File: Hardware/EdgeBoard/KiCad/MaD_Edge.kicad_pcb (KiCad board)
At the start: 4 copper layers, 144.1 x 93.3 mm, 281 parts, among them IC1 ISO6742DWR, IC10 NSI50010YT1G, IC11 NSI50010YT1G, IC12 NSI50010YT1G, IC13 NSI50010YT1G, IC14 ISO7741FDWR, IC15 ISO6721BDR, IC16 ISO6740FDWR, IC2 ISO6742DWR, IC3 UCC12040DVER, IC4 UCC12040DVER, IC5 ISO6731DWR, IC6 NSI50010YT1G, IC7 NSI50010YT1G, IC8 NSI50010YT1G, IC9 NSI50010YT1G, J1 Debug, J10 ChargePump, J11 ESDUpper, J12 ESDLower, J13 ESDActive, J14 ENDUpper, J15 ENDLower, J16 Door, J17 GPI_3, J18 GPI_4, J19 NavKey, J2 Main_Power, J20 Encoder, J21 ServoCtrl, J22 GPIO_EXT_1, J23 ServoSerial, J24 GPIO_EXT_2, J3 P2_EDGE_MODULE_SOCKET, J4 436500321, J5 GPO_2, J6 GPO_1, J7 GPI_2, J8 GPI_1, J9 Force, Q1 MMBT3904, SW1 RESET, U1 XL1509-5V, U10 SN74LVC1G14DBV, U11 SN74LVC1G14DBV, U12 SN74LVC1G14DBV, U13 SN74LVC1G14DBV, U14 SN74LVC1G14DBV, U15 SN74LVC1G14DBV, U16 SN74LVC1G14DBV, U17 SN74LVC1G14DBV, U18 SN74LVC1G14DBV, U19 SN74LVC1G14DBV, U2 XL1509-3.3V, U21 SN74LVC1G14DBV, U22 SN74LVC1G14DBV, U24 AM26LS31CD, U25 AM26C32IDR, U27 SN74LVC1G14DBV, U28 SN74LVC1G14DBV, U29 SN74LVC1G14DBV, U3 APM4953, U30 SN74LVC1G14DBV, U31 SN74LVC1G14DBV, U32 SN74LVC1G14DBV, U33 SN74LVC1G14DBV, U34 SN74LVC1G14DBV, U4 6N137, U5 VO2631, U6 VO2631, U7 VO2631, U8 VO2631, U9 SN74LVC1G14DBV

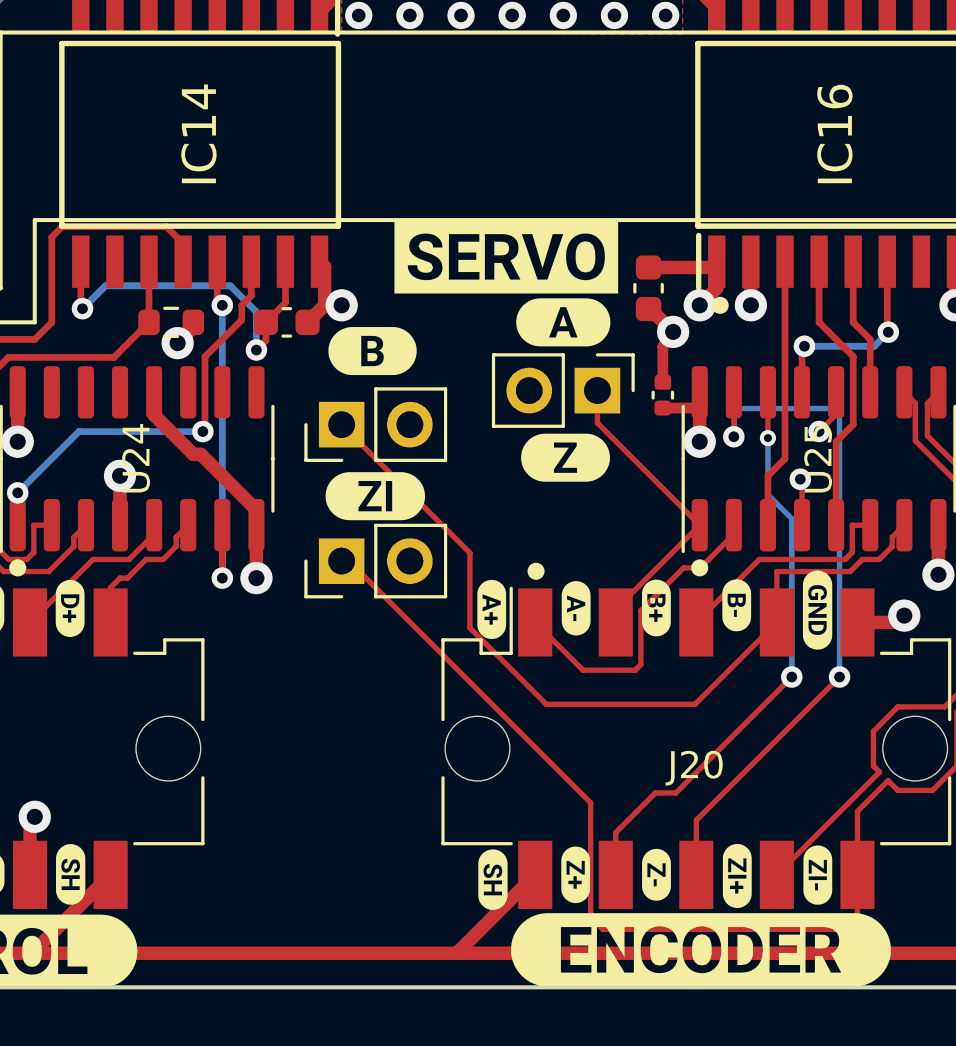
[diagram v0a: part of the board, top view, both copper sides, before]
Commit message: feat(hardware): encoder front end for single-ended and open-collector encoders
Findings ENC-F4a and ENC-F4b. Grounding a minus input can never give the
-0.2 V differential low (SLLS104M 5.6 p.5), and the Taiss NPN
open-collector encoder had no pull-up and no supply.

- JP2/JP3/JP5 now tie A-/B-/ZI- to ENC_REF instead of EN_GND (values
  A_REF/B_REF/ZI_REF); JP6 (Z_REF) is the Z- jumper where JP4 was.
- ENC_REF = SC_5V/2: R43/R44 2.2 k, C31 0.1 uF, placed between IC14 and
  IC16; B.Cu to the four jumpers.
- R40/R41/R42 2.2 k pull-ups on A+/B+/Z+ (an A/B/Z encoder). Placed
  between J21 and J20, tapped onto the + nets with vias and B.Cu.
- J25 (1x3 header: VIN, fused +V, 0V) with F1, Littelfuse 1206L020/30NR
  (C7542932; 0.20 A hold, 30 V, 1206L datasheet p.1), as an external
  supply pass-through: J20 has no free pin and the encoder side only has
  SC_5V from the drive.
- BOM: SH1-SH4, 2.54 mm shunts (HC-JP254-1-65-CL-B-G0, C5380290) for
  JP1 (always) and JP2/JP3/JP6 (open-collector encoder only), as
  BOM-only symbols.
- Silkscreen: SERVO label moved up 2.2 mm; VIN/+V/0V at J25; SHUNT=OC
  between the jumpers.

Co-Authored-By: Claude Opus 5.5 <noreply@anthropic.com>
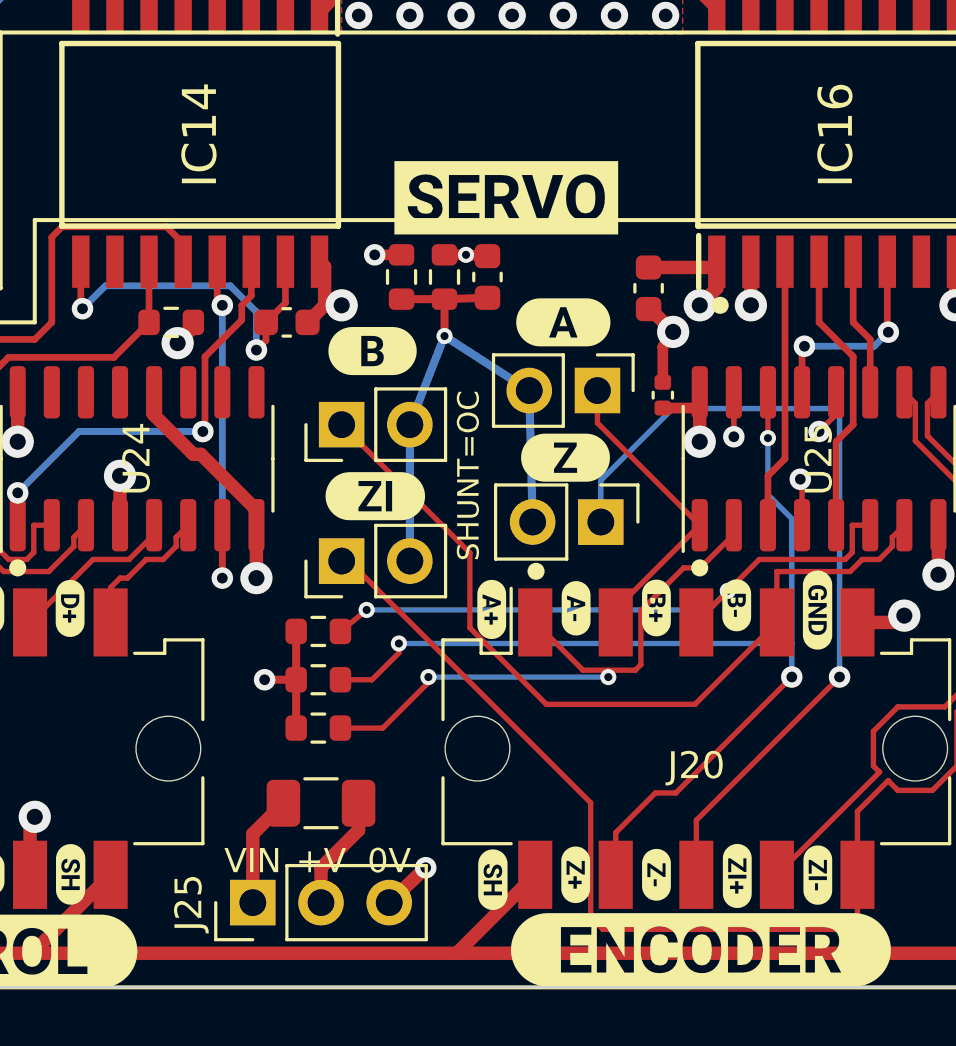
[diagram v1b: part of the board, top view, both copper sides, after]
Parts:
- added C31: 0.1uF, Capacitor_SMD:C_0603_1608Metric, F.Cu at (44.8, 185.0)
- added F1: 0.2A/30V, Fuse:Fuse_1206_3216Metric, F.Cu at (38.6, 204.6)
- added J25: ENC_PWR, Connector_PinHeader_2.54mm:PinHeader_1x03_P2.54mm_Vertical, F.Cu at (36.1, 208.3)
- added JP6: Z_REF, Connector_PinHeader_2.54mm:PinHeader_1x02_P2.54mm_Vertical, F.Cu at (49.0, 194.1)
- added R40: 2.2K, Resistor_SMD:R_0603_1608Metric, F.Cu at (38.5, 201.8)
- added R41: 2.2K, Resistor_SMD:R_0603_1608Metric, F.Cu at (38.5, 198.2)
- added R42: 2.2K, Resistor_SMD:R_0603_1608Metric, F.Cu at (38.5, 200.0)
- added R43: 2.2K, Resistor_SMD:R_0603_1608Metric, F.Cu at (41.6, 185.0)
- added R44: 2.2K, Resistor_SMD:R_0603_1608Metric, F.Cu at (43.2, 185.0)
- JP2: value A_GND -> A_REF
- JP3: value B_GND -> B_REF
- JP5: value ZI_GND -> ZI_REF
- moved kibuzzard-6474D3A4 2.20 mm to (45.5, 182.1)
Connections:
- JP2 pad 2: /MaD_Edge_Sheet3/EN_GND -> /MaD_Edge_Sheet3/ENC_REF
- JP3 pad 2: /MaD_Edge_Sheet3/EN_GND -> /MaD_Edge_Sheet3/ENC_REF
- JP5 pad 2: /MaD_Edge_Sheet3/EN_GND -> /MaD_Edge_Sheet3/ENC_REF
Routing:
- net /MaD_Edge_Sheet3/ENC_REF: track 0.00 -> 21.8 mm, vias 0 -> 1
- net /MaD_Edge_Sheet3/Z+: track 21.5 -> 39.1 mm, vias 2 -> 3
- net /MaD_Edge_Sheet3/B+: track 8.57 -> 23.6 mm, vias 0 -> 2
- net /MaD_Edge_Sheet3/A+: track 11.7 -> 22.9 mm, vias 0 -> 2
- net /MaD_Edge_Sheet3/Z-: track 26.2 -> 33.8 mm
- net /MaD_Edge_Sheet3/SC_5V: track 19.7 -> 25.5 mm, vias 8 -> 10
- net /MaD_Edge_Sheet3/ENC_V+: track 0.00 -> 4.28 mm
- net /MaD_Edge_Sheet3/ENC_VIN: track 0.00 -> 4.17 mm
- net /MaD_Edge_Sheet3/EN_GND: track 40.4 -> 43.8 mm, vias 12 -> 14
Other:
- board text added: "+V"
- board text added: "0V"
- board text added: "SHUNT=OC"
- board text added: "VIN"

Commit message: fix(hardware): Pi link on P29-P32 and a 3.3 V Pi side
Findings HOST-F2 and HOST-F5. The P2-EC32MB does not bring out P40-P57
(fingers 59-62 are no-connects), so IC2 on P52-P55 was dead, and the Pi
side ran from 5 V, putting about 5 V on Pi GPIO.

- IC2 INA/INB/OUTC/OUTD move to P32/P31/P30/P29. P29-P31 are the only
  EC32MB pins the carrier leaves unused; the fourth (an isolator input,
  10 uA max, SLLSFJ6G p.12) shares P32 with J22.3.
- Routes: the old P52-P55 copper is removed; IC2 to four vias, B.Cu down
  to J22.3 (P32) and to vias in J3 fingers 9-11 (the only access).
- RPI_5V renamed RPI_3V3 (pads, tracks, In2 plane); J4.1 silkscreen
  reads 3V3. ISO674x runs at 2.25-5.5 V with VIT+ = 0.7 VCCI (SLLSFJ6G
  p.8, p.12).
- IC2 alternate ISO7742FDWR dropped: a default-low output would hold the
  UART low (SLLSFJ6G p.31).

Firmware follow-up: HW_PIN_RPI_TX 55 -> 32, HW_PIN_RPI_RX 53 -> 30.

Co-Authored-By: Claude Opus 5.5 <noreply@anthropic.com>
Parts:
- removed kibuzzard-6477790B: G***, kibuzzard-6477790B
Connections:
- net /MaD_Edge_Sheet2/RPI_5V renamed /MaD_Edge_Sheet2/RPI_3V3
- IC2 pad 3: P55 -> P32
- IC2 pad 4: P54 -> P31
- IC2 pad 5: P53 -> P30
- IC2 pad 6: P52 -> P29
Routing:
- net P32: track 3.09 -> 56.9 mm, vias 0 -> 1
- net P29: track 0.00 -> 53.8 mm, vias 0 -> 2
- net P30: track 0.00 -> 53.2 mm, vias 0 -> 2
- net P31: track 0.00 -> 52.6 mm, vias 0 -> 2
- net P55: track 49.3 -> 0.00 mm
- net P54: track 47.5 -> 0.00 mm
- net P52: track 46.9 -> 0.00 mm
- net P53: track 45.9 -> 0.00 mm

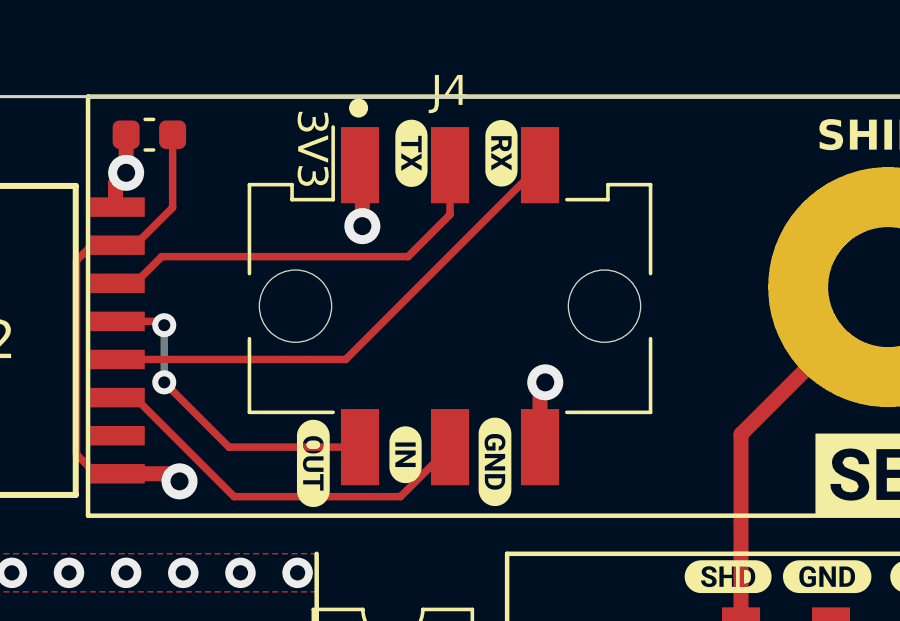
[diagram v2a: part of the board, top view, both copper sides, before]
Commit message: fix(hardware): J4 back on the 43045-0618 footprint
Finding HOST-J4. J4's BOM part is 0430450618 (with solder tabs) and the
2023 board used the 43045-0618 footprint; the current files had 0615
(no tabs). The library footprint drops in at the same place: its two
mounting pads clear all copper (checked against every F.Cu item with
0.2 mm clearance). The tabs stay unnumbered as in 2023, so the DRC
parity note about J4 pin 7 (SHIELD) is unchanged.

Co-Authored-By: Claude Opus 5.5 <noreply@anthropic.com>
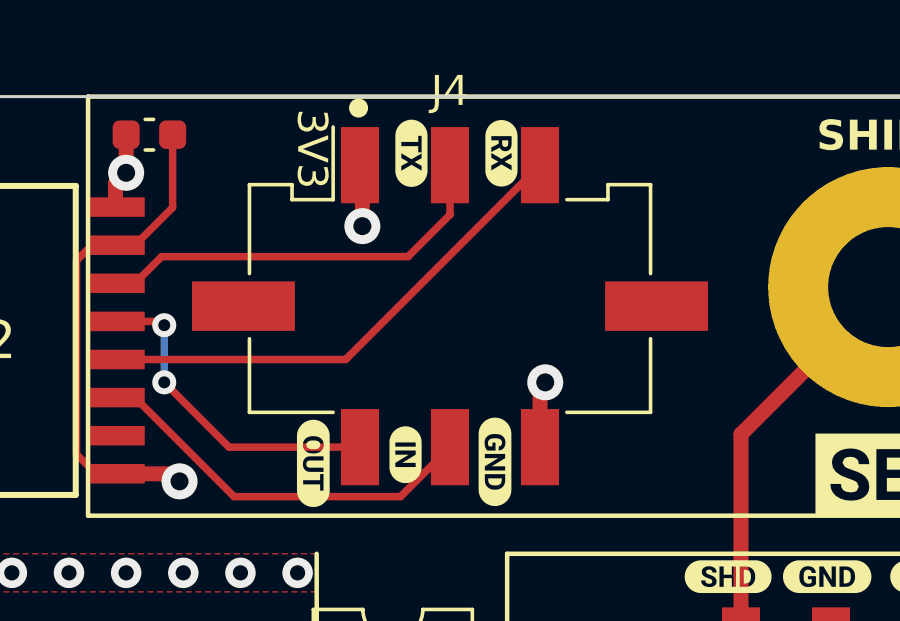
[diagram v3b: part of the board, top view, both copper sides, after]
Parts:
- J4: footprint Connector_Molex:Molex_Micro-Fit_3.0_43045-0615_2x03_P3.00mm_Vertical -> Connector_Molex:Molex_Micro-Fit_3.0_43045-0618_2x03-1MP_P3.00mm_Vertical

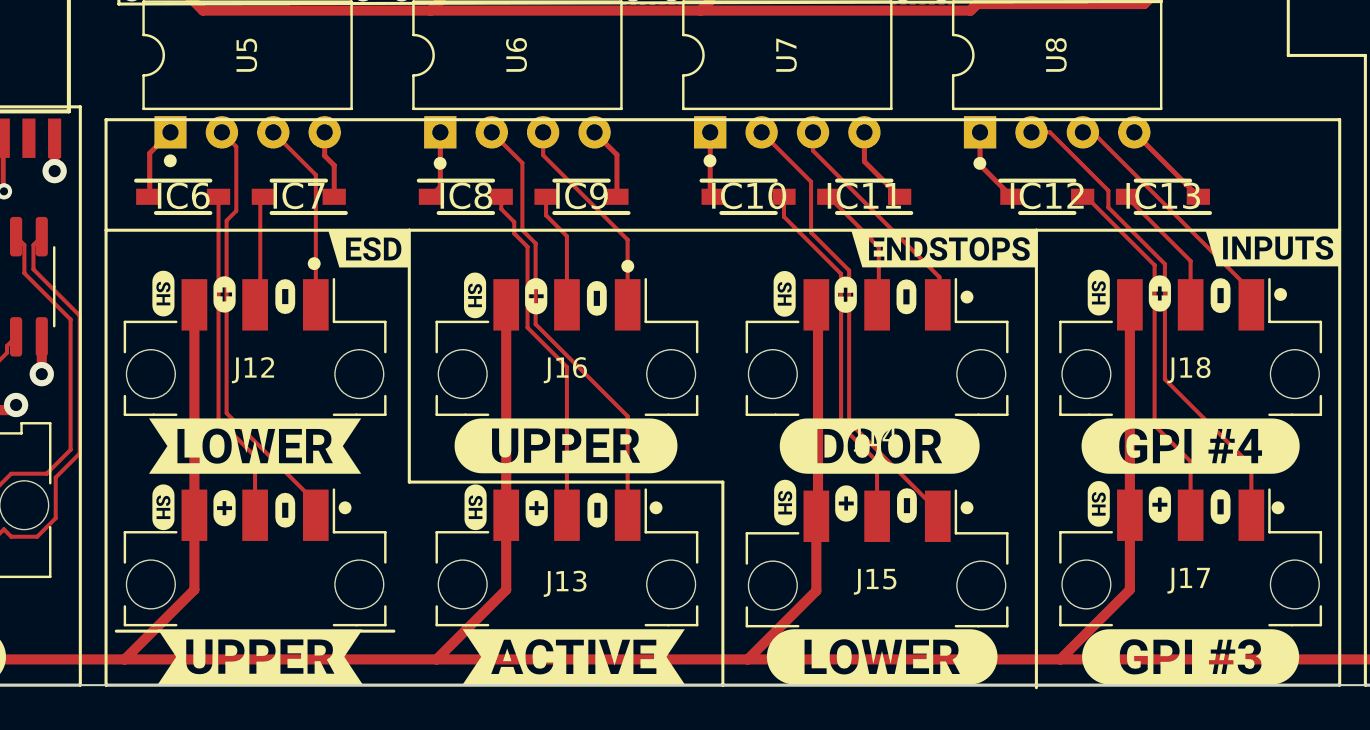
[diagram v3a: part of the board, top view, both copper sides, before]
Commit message: fix(hardware): copper on the NSI50010 loop regulators; supported loop range
Finding REST-F7d. On almost no copper the NSI50010s (IC6-IC13) run over
their rating on 24 V loops (onsemi NSI50010Y/D Rev 3 p.3: 208 mW on
100 mm2 of 1 oz copper).

- A B.Cu pour on each cathode net, three 0.6 mm vias from the cathode
  pad: 138-231 mm2 per part (zone fill), against about 5 mm2 before.
- A series resistor was not used: a 5 V loop leaves 5 - 1.7 V (VO2631
  VF max) for the regulator, which needs 1.8 V, so at most about 115 ohm
  could be added, which saves only about 20 mW at 24 V.
- Supported loop supply: 5-12 V (worst case to 65 C), 15 V to 40 C,
  not 24 V. The pours are credited only as the datasheet's 100 mm2 case
  (conservative). See the readme.

Co-Authored-By: Claude Opus 5.5 <noreply@anthropic.com>
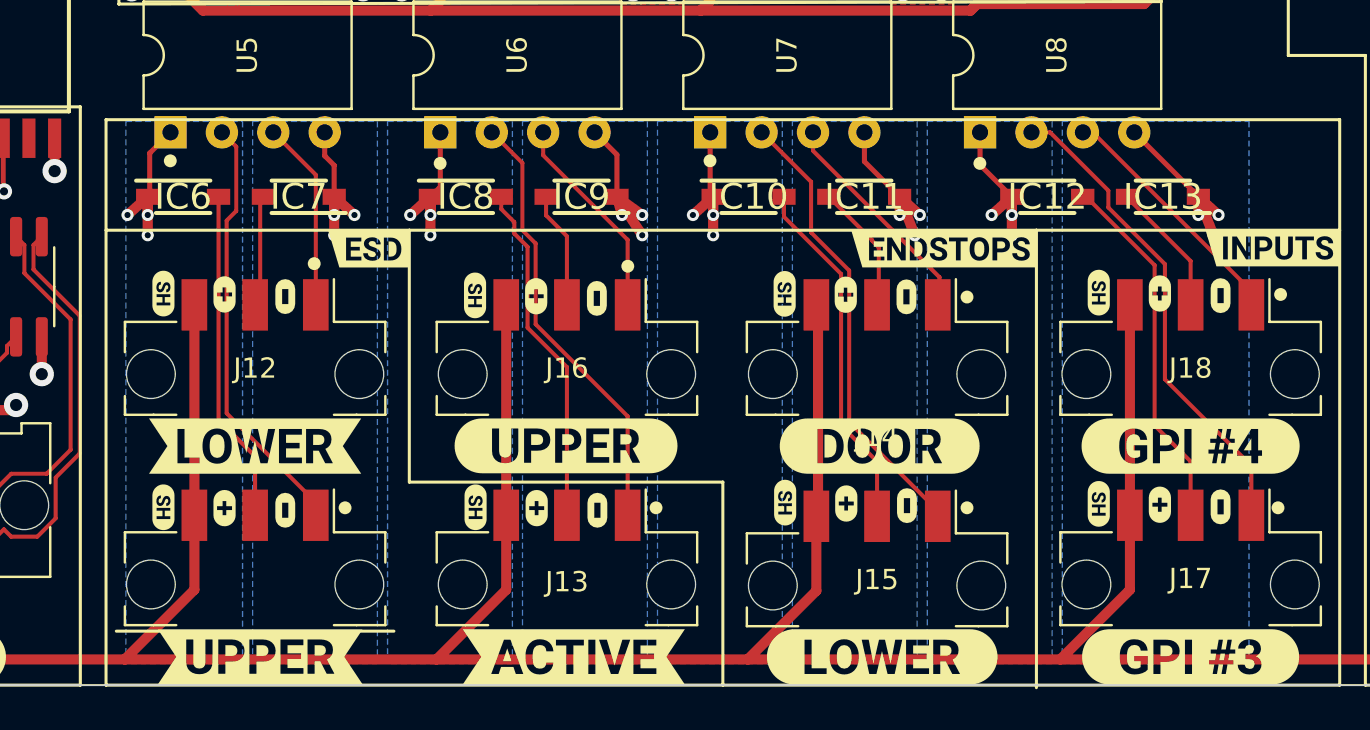
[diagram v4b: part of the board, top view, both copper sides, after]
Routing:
- net Net-(IC9-K): track 3.64 -> 8.39 mm, vias 0 -> 3
- net Net-(IC11-K): track 3.91 -> 8.19 mm, vias 0 -> 3
- net Net-(IC13-K): track 4.50 -> 8.78 mm, vias 0 -> 3
- net Net-(IC8-K): track 3.39 -> 7.53 mm, vias 0 -> 3
- net Net-(IC7-K): track 3.38 -> 7.53 mm, vias 0 -> 3
- net Net-(IC6-K): track 3.65 -> 7.80 mm, vias 0 -> 3
- net Net-(IC12-K): track 3.84 -> 7.98 mm, vias 0 -> 3
- net Net-(IC10-K): track 3.25 -> 7.39 mm, vias 0 -> 3
- added copper zone on B.Cu, net Net-(IC10-K)
- added copper zone on B.Cu, net Net-(IC11-K)
- added copper zone on B.Cu, net Net-(IC12-K)
- added copper zone on B.Cu, net Net-(IC13-K)
- added copper zone on B.Cu, net Net-(IC6-K)
- added copper zone on B.Cu, net Net-(IC7-K)
- added copper zone on B.Cu, net Net-(IC8-K)
- added copper zone on B.Cu, net Net-(IC9-K)
